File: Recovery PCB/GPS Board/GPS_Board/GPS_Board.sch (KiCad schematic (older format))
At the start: 13 parts, among them J1 XT30-M, J2 XT30-M, U1 Teensy4.1

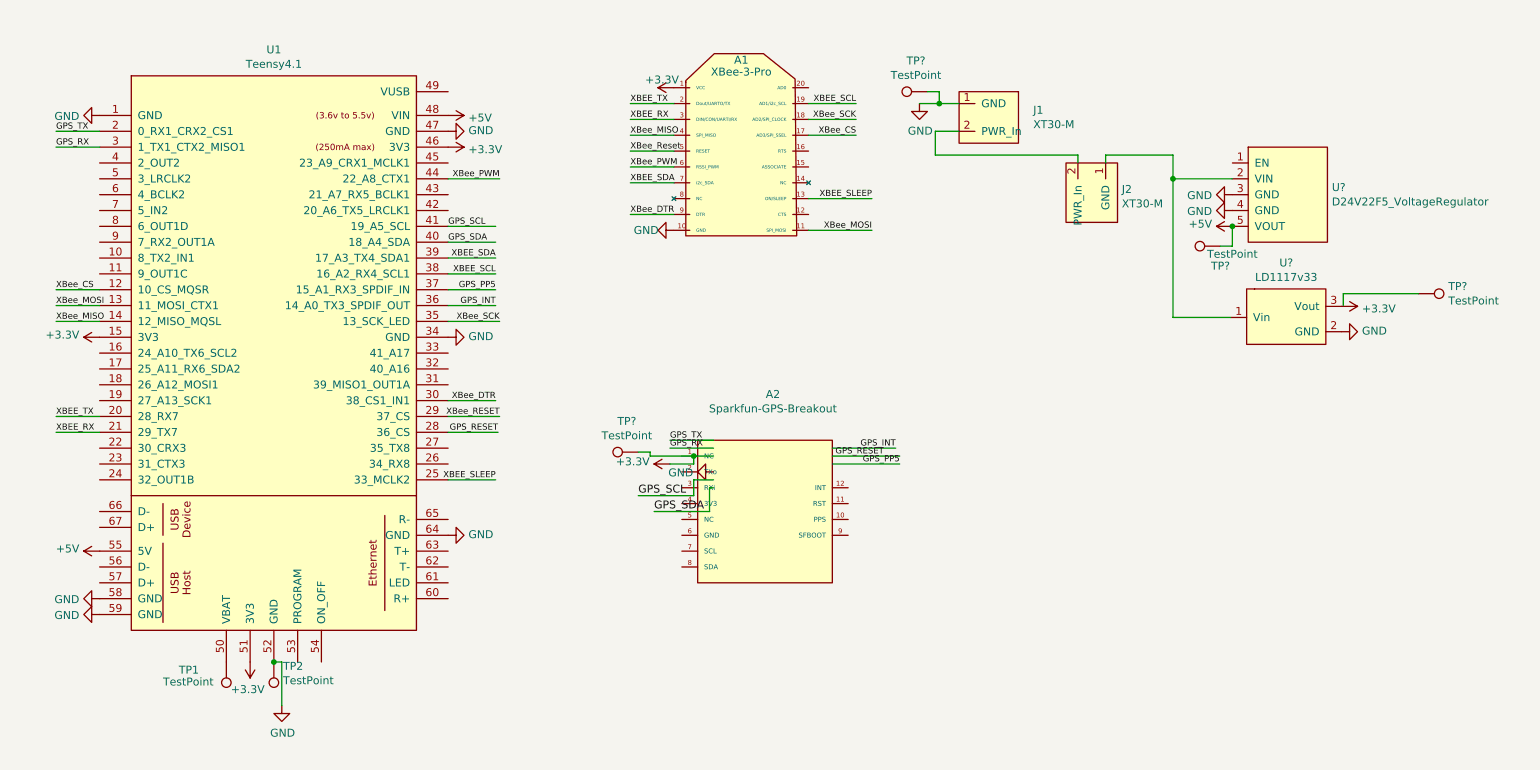
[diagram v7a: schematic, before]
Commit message: Fixed GPS symbol
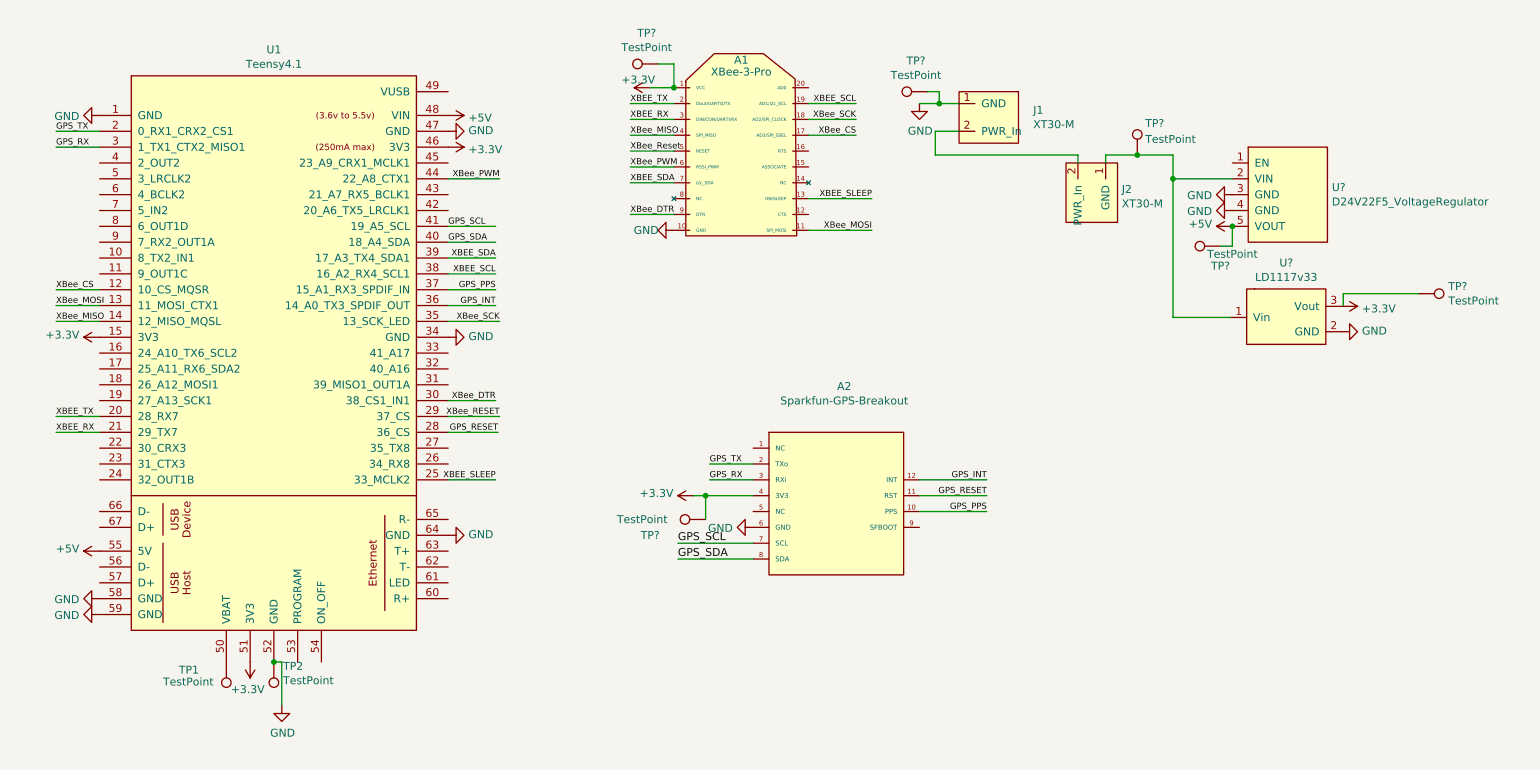
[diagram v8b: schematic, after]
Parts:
- added TP? (x2): TestPoint, symbol Connector:TestPoint
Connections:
- net labels added: GPS_PPS
- net labels removed: GPS_PP5
- wire segments 68 -> 65
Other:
- moved on the sheet: A2, TP?
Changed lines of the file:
@@
 	8150 1700 8150 1650
 Wire Wire Line
-	8150 1650 8575 1650
+	8150 1650 8350 1650
 Wire Wire Line
 	8575 1650 8575 1800
 Wire Wire Line
 	6975 1325 7100 1325
-$Comp
-L GPS_Board:Sparkfun-GPS-Breakout A2
-U 1 1 61AAF79D
-P 6000 3900
-F 0 "A2" H 6050 4640 50  0000 C CNN
-F 1 "Sparkfun-GPS-Breakout" H 6050 4549 50  0000 C CNN
-F 2 "GPS Board:Sparkfun-GPS-ZOE-M8Q-Breakout" H 6000 3900 50  0001 C CNN
-F 3 "" H 6000 3900 50  0001 C CNN
-	1    6000 3900
-	1    0    0    -1
-$EndComp
-Wire Wire Line
-	5400 3450 5675 3450
-Wire Wire Line
-	5400 3500 5675 3500
+Wire Wire Line
+	5650 3700 5925 3700
 $Comp
 L power:GND #PWR0101
 U 1 1 61ABCD1D
-P 5675 3650
-F 0 "#PWR0101" H 5675 3400 50  0001 C CNN
-F 1 "GND" V 5680 3522 50  0000 R CNN
-F 2 "" H 5675 3650 50  0001 C CNN
-F 3 "" H 5675 3650 50  0001 C CNN
-	1    5675 3650
+P 5925 4000
+F 0 "#PWR0101" H 5925 3750 50  0001 C CNN
+F 1 "GND" V 5930 3872 50  0000 R CNN
+F 2 "" H 5925 4000 50  0001 C CNN
+F 3 "" H 5925 4000 50  0001 C CNN
+	1    5925 4000
 	0    1    1    0
 $EndComp
@@
 Wire Wire Line
 	4000 2200 4300 2200
-Wire Wire Line
-	5300 3900 5650 3900
-Wire Wire Line
-	5550 3700 5550 3800
-Wire Wire Line
-	5550 3800 5200 3800
-Wire Wire Line
-	5675 3700 5550 3700
-Wire Wire Line
-	5650 3750 5650 3900
-Wire Wire Line
-	5650 3750 5675 3750
 Text Label 4000 2100 0    39   ~ 0
 GPS_SCL
 Text Label 4000 2200 0    39   ~ 0
 GPS_SDA
-Text Label 5200 3800 0    50   ~ 0
+Text Label 5450 4100 0    50   ~ 0
 GPS_SCL
-Text Label 5300 3900 0    50   ~ 0
+Text Label 5450 4200 0    50   ~ 0
 GPS_SDA
 Wire Wire Line
 	4000 2100 4300 2100
-Wire Wire Line
-	5550 3550 5675 3550
-Wire Wire Line
-	5550 3550 5550 3600
-Wire Wire Line
-	5550 3600 5400 3600
 $Comp
 L power:+3.3V #PWR?
 U 1 1 625F178F
-P 5400 3600
-F 0 "#PWR?" H 5400 3450 50  0001 C CNN
-F 1 "+3.3V" V 5415 3728 50  0000 L CNN
-F 2 "" H 5400 3600 50  0001 C CNN
-F 3 "" H 5400 3600 50  0001 C CNN
-	1    5400 3600
+P 5550 3800
+F 0 "#PWR?" H 5550 3650 50  0001 C CNN
+F 1 "+3.3V" V 5565 3928 50  0000 L CNN
+F 2 "" H 5550 3800 50  0001 C CNN
+F 3 "" H 5550 3800 50  0001 C CNN
+	1    5550 3800
 	0    -1   -1   0
 $EndComp
@@
 Wire Wire Line
 	4000 3400 4315 3400
-Text Label 6750 3550 2    39   ~ 0
+Text Label 7400 3800 2    39   ~ 0
 GPS_RESET
 Wire Wire Line
-	6425 3550 6850 3550
-Wire Wire Line
-	6425 3600 6850 3600
+	6975 3800 7400 3800
+Wire Wire Line
+	6975 3900 7400 3900
 Text Label 4300 2500 2    39   ~ 0
-GPS_PP5
+GPS_PPS
 Wire Wire Line
 	4000 2500 4300 2500
-Text Label 6850 3600 2    39   ~ 0
-GPS_PP5
-Wire Wire Line
-	6425 3500 6825 3500
+Text Label 7400 3900 2    39   ~ 0
+GPS_PPS
 Wire Wire Line
 	4000 2600 4300 2600
 Text Label 4300 2600 2    39   ~ 0
 GPS_INT
-Text Label 6825 3500 2    39   ~ 0
+Text Label 7400 3700 2    39   ~ 0
 GPS_INT
 Text Label 4325 2700 2    39   ~ 0
@@
 L power:+3.3V #PWR?
 U 1 1 625CE6B8
-P 5425 1225
-F 0 "#PWR?" H 5425 1075 50  0001 C CNN
-F 1 "+3.3V" V 5475 1300 50  0000 C CNN
-F 2 "" H 5425 1225 50  0001 C CNN
-F 3 "" H 5425 1225 50  0001 C CNN
-	1    5425 1225
+P 5275 1225
+F 0 "#PWR?" H 5275 1075 50  0001 C CNN
+F 1 "+3.3V" V 5325 1300 50  0000 C CNN
+F 2 "" H 5275 1225 50  0001 C CNN
+F 3 "" H 5275 1225 50  0001 C CNN
+	1    5275 1225
 	0    -1   -1   0
 $EndComp
@@
 Text Label 1525 3400 0    39   ~ 0
 XBEE_RX
-Text Label 5400 3450 0    39   ~ 0
-GPS_TX
-Text Label 5400 3500 0    39   ~ 0
-GPS_RX
 Wire Wire Line
 	1800 1500 1525 1500
@@
 	0    -1   -1   0
 $EndComp
-Wire Wire Line
-	5550 3550 5275 3550
-Wire Wire Line
-	5275 3550 5275 3525
-Wire Wire Line
-	5275 3525 5200 3525
-Connection ~ 5550 3550
 $Comp
 L Connector:TestPoint TP?
 U 1 1 625F3DB9
-P 5200 3525
-F 0 "TP?" V 5395 3597 50  0000 C CNN
-F 1 "TestPoint" V 5304 3597 50  0000 C CNN
-F 2 "" H 5400 3525 50  0001 C CNN
-F 3 "~" H 5400 3525 50  0001 C CNN
-	1    5200 3525
+P 5625 3950
+F 0 "TP?" V 5525 4300 50  0000 C CNN
+F 1 "TestPoint" V 5625 4350 50  0000 C CNN
+F 2 "" H 5825 3950 50  0001 C CNN
+F 3 "~" H 5825 3950 50  0001 C CNN
+	1    5625 3950
 	0    -1   -1   0
 $EndComp
@@
 	0    -1   -1   0
 $EndComp
+Wire Wire Line
+	5450 4200 5925 4200
+Wire Wire Line
+	5450 4100 5925 4100
+Text Label 5650 3700 0    39   ~ 0
+GPS_RX
+Wire Wire Line
+	5650 3600 5925 3600
+Text Label 5650 3600 0    39   ~ 0
+GPS_TX
+Wire Wire Line
+	5925 3800 5625 3800
+$Comp
+L GPS_Board:Sparkfun-GPS-Breakout A2
+U 1 1 61AAF79D
+P 6450 3850
+F 0 "A2" H 6500 4590 50  0000 C CNN
+F 1 "Sparkfun-GPS-Breakout" H 6500 4499 50  0000 C CNN
+F 2 "GPS Board:Sparkfun-GPS-ZOE-M8Q-Breakout" H 6450 3850 50  0001 C CNN
+F 3 "" H 6450 3850 50  0001 C CNN
+	1    6450 3850
+	1    0    0    -1
+$EndComp
+Wire Wire Line
+	5625 3800 5625 3950
+Connection ~ 5625 3800
+Wire Wire Line
+	5625 3800 5550 3800
+Wire Wire Line
+	6975 3700 7400 3700
+Wire Wire Line
+	5275 1225 5425 1225
+Wire Wire Line
+	5425 1225 5425 1075
+Connection ~ 5425 1225
+$Comp
+L Connector:TestPoint TP?
+U 1 1 62601ADB
+P 5325 1075
+F 0 "TP?" V 5520 1147 50  0000 C CNN
+F 1 "TestPoint" V 5429 1147 50  0000 C CNN
+F 2 "" H 5525 1075 50  0001 C CNN
+F 3 "~" H 5525 1075 50  0001 C CNN
+	1    5325 1075
+	0    -1   -1   0
+$EndComp
+Wire Wire Line
+	5325 1075 5425 1075
+$Comp
+L Connector:TestPoint TP?
+U 1 1 626043C8
+P 8350 1650
+F 0 "TP?" H 8400 1850 50  0000 L CNN
+F 1 "TestPoint" H 8400 1750 50  0000 L CNN
+F 2 "" H 8550 1650 50  0001 C CNN
+F 3 "~" H 8550 1650 50  0001 C CNN
+	1    8350 1650
+	1    0    0    -1
+$EndComp
+Connection ~ 8350 1650
+Wire Wire Line
+	8350 1650 8575 1650
 $EndSCHEMATC
